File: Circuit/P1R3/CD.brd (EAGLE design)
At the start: 50.8 x 50.8 mm, 75 parts, among them U1 MK20DX256VLH7, U2 TPS61200, U3 MPU-9250, Y1 32.768KHz, Y2 16Mhz/8pF, Y3 26 Mhz, Y4 16 Mhz

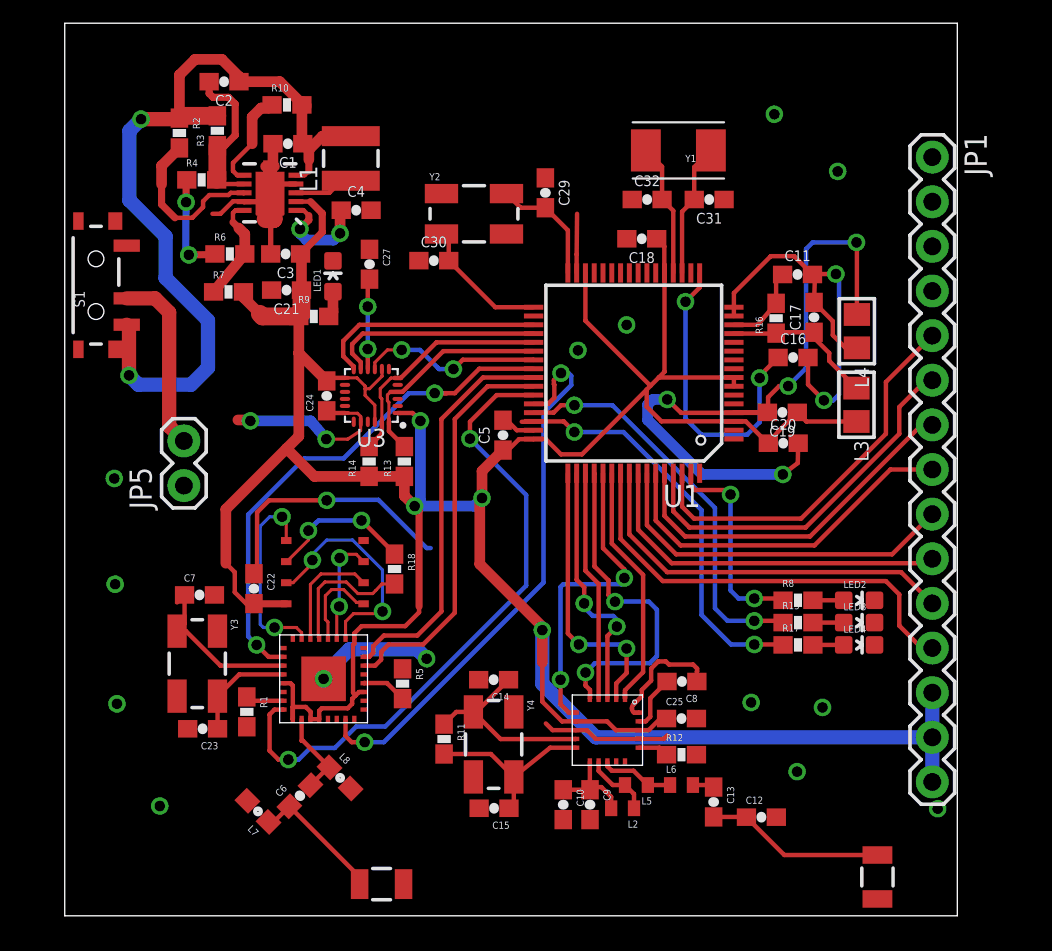
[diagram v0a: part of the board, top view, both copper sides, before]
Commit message: Preliminary R4 board done, latest named as CD in P1R4 directory
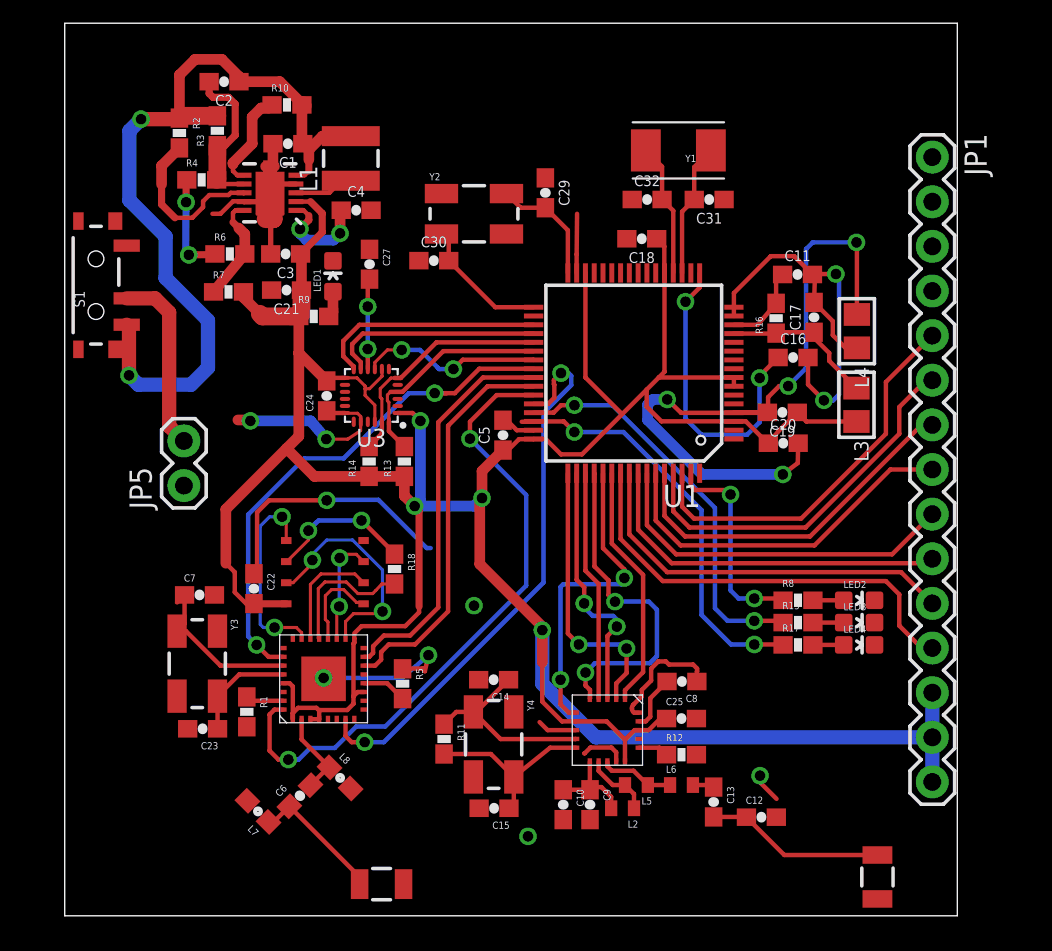
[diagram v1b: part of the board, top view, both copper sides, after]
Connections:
- net 3.3V: now also U$4.15
- net GND: now also U$4.14
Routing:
- net 3.3V: track 188.3 -> 190.8 mm
- net GND: track 111.1 -> 111.6 mm, vias 11 -> 13
